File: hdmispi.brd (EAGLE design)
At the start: 30.5 x 25.4 mm, 3 parts

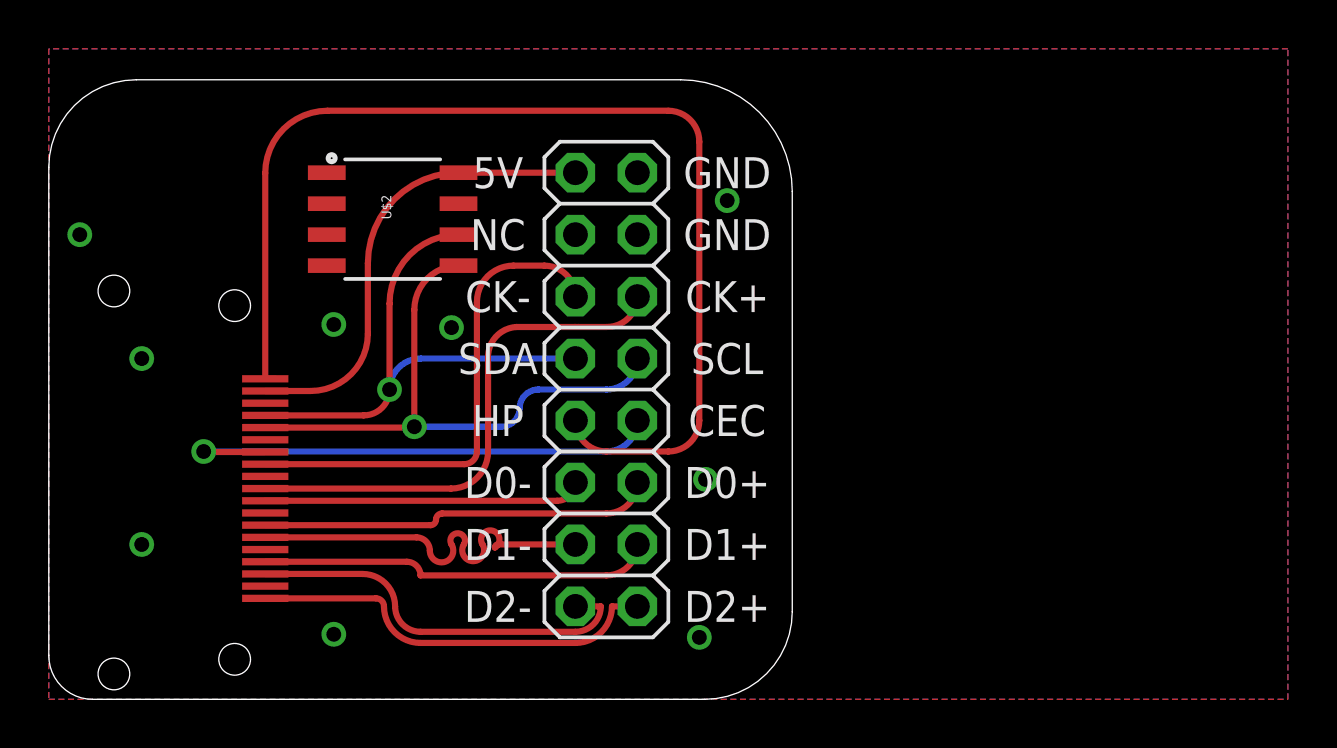
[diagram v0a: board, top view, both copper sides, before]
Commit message: next rev of files, v1.0. Switched SDA/SCL wires by accident, doesn't work.
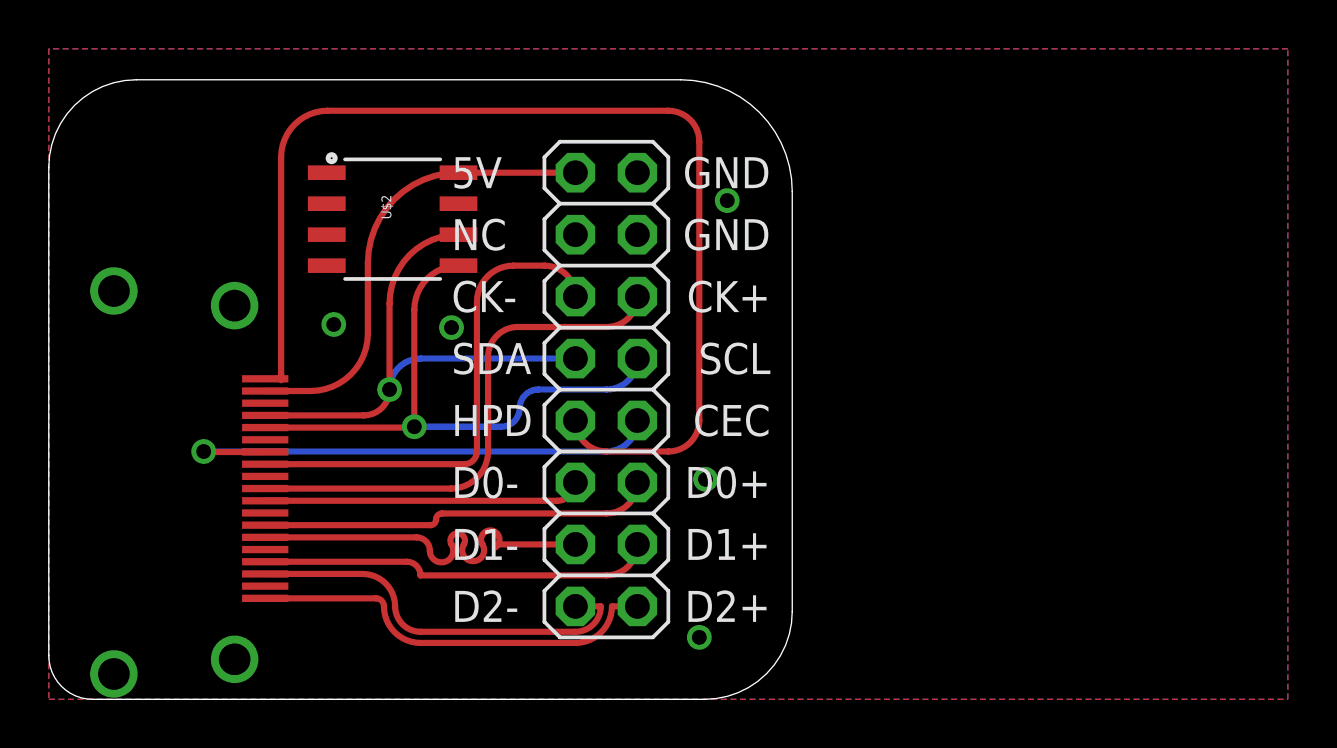
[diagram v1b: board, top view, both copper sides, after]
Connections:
- net GND: now also U$1.P$20, U$1.P$21, U$1.P$22, U$1.P$23
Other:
- board text added: "5V NC CK- SDA HPD D0- D1- D2-"
- board text added: "joefitz@securinghardware.com HDMI Breakout v1.0 W/ Microchip 24LC00/SN I2C EEPROM for EDID"
- board text removed: "5V NC CK- SDA HP D0- D1- D2-"
- board text removed: "joefitz@securinghardware.com HDMI Breakout v1.0 With Microchip 24LC00/SN I2C EEPROM for EDID"
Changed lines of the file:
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@@
 <text x="10.922" y="21.336" size="1.016" layer="26" rot="MR180" align="center">joefitz@securinghardware.com
 HDMI Breakout v1.0
-With Microchip 24LC00/SN
+W/ Microchip 24LC00/SN
 I2C EEPROM for EDID</text>
-<text x="18.415" y="12.7" size="1.27" layer="25" distance="100" rot="R180" align="center">5V
+<text x="16.51" y="12.7" size="1.27" layer="25" distance="100" rot="R180" align="center-right">5V
 NC
 CK-
 SDA
-HP
+HPD
 D0-
 D1-
 D2-</text>
-<text x="27.813" y="12.7" size="1.27" layer="25" distance="100" rot="R180" align="center">GND
+<text x="29.591" y="12.7" size="1.27" layer="25" distance="100" rot="R180" align="center-left">GND
 GND
 CK+
@@
 </polygon>
 <via x="26.67" y="2.54" extent="1-16" drill="0.6096" shape="square"/>
-<via x="3.81" y="6.35" extent="1-16" drill="0.6096" shape="square"/>
-<via x="3.81" y="13.97" extent="1-16" drill="0.6096" shape="square"/>
-<via x="1.27" y="19.05" extent="1-16" drill="0.6096" shape="square"/>
 <via x="16.51" y="15.24" extent="1-16" drill="0.6096" shape="square"/>
 <via x="27.813" y="20.447" extent="1-16" drill="0.6096" shape="square"/>
 <via x="11.684" y="15.367" extent="1-16" drill="0.6096" shape="square"/>
-<via x="11.684" y="2.667" extent="1-16" drill="0.6096" shape="square"/>
 <via x="26.924" y="9.017" extent="1-16" drill="0.6096" shape="square"/>
 <contactref element="U$2" pad="4"/>
+<contactref element="U$1" pad="P$23"/>
+<contactref element="U$1" pad="P$22"/>
+<contactref element="U$1" pad="P$21"/>
+<contactref element="U$1" pad="P$20"/>
 </signal>
 <signal name="TMDSC_N">
@@
 <wire x1="25.4" y1="24.13" x2="11.43" y2="24.13" width="0.254" layer="1"/>
 <wire x1="8.874" y1="13.14" x2="9.33" y2="13.14" width="0.254" layer="1"/>
-<wire x1="11.43" y1="24.13" x2="8.874" y2="21.574" width="0.254" layer="1" curve="90"/>
-<wire x1="8.874" y1="21.574" x2="8.874" y2="13.14" width="0.254" layer="1"/>
+<wire x1="11.43" y1="24.13" x2="9.525" y2="22.225" width="0.254" layer="1" curve="90"/>
+<wire x1="9.525" y1="22.225" x2="9.525" y2="13.97" width="0.254" layer="1"/>
+<wire x1="9.525" y1="13.335" x2="9.525" y2="13.081" width="0.254" layer="1"/>
+<wire x1="9.33" y1="13.14" x2="9.525" y2="13.335" width="0.254" layer="1" curve="90"/>
+<wire x1="9.525" y1="13.335" x2="9.525" y2="13.97" width="0.254" layer="1"/>
 </signal>
 <signal name="TMDS0_N">

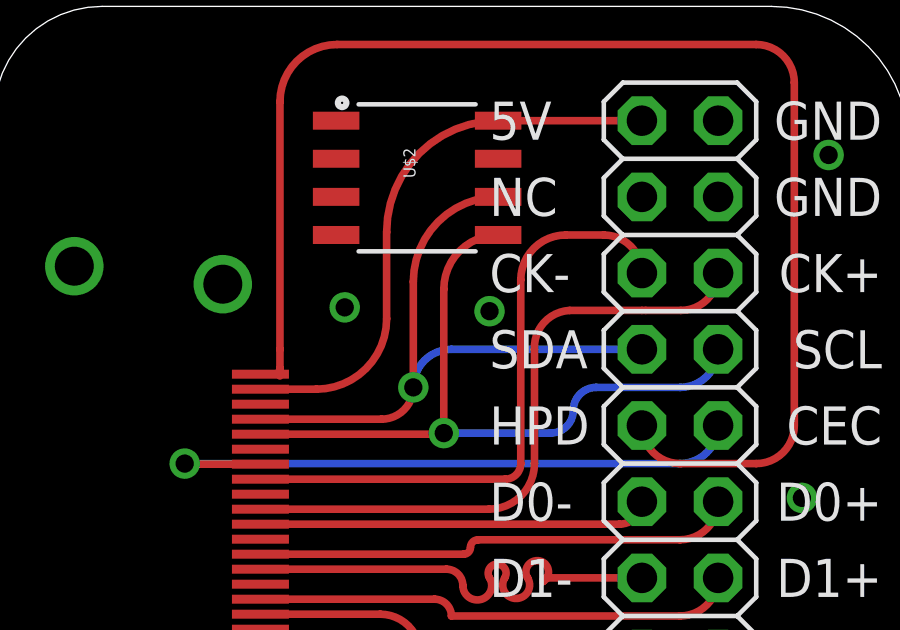
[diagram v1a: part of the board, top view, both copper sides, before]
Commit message: fixed board and schematic with sda/scl corrected.
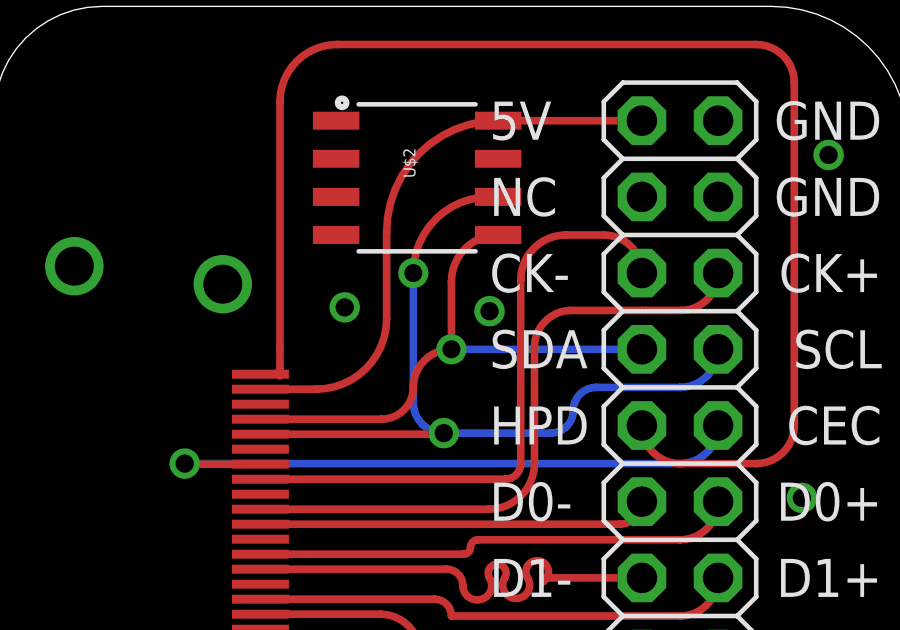
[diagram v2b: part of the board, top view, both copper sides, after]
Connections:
- net DDC_CK: now also U$2.6; no longer U$2.5
- net DDC_D: now also U$2.5; no longer U$2.6
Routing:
- net DDC_D: track 21.2 -> 18.1 mm
- net DDC_CK: track 23.8 -> 26.1 mm, vias 1 -> 2
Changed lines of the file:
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@@
 <?xml version="1.0" encoding="utf-8"?>
 <!DOCTYPE eagle SYSTEM "eagle.dtd">
-<eagle version="7.2.0">
+<eagle version="7.6.0">
 <drawing>
 <settings>
@@
 <contactref element="JP1" pad="7"/>
 <contactref element="U$1" pad="P$16"/>
+<contactref element="U$2" pad="5"/>
 <wire x1="8.874" y1="11.64" x2="12.91" y2="11.64" width="0.254" layer="1"/>
 <wire x1="12.91" y1="11.64" x2="13.97" y2="12.7" width="0.254" layer="1" curve="90"/>
-<via x="13.97" y="12.7" extent="1-16" drill="0.6096" shape="square"/>
-<wire x1="13.97" y1="12.7" x2="15.24" y2="13.97" width="0.254" layer="16" curve="-90"/>
+<wire x1="13.97" y1="12.7" x2="15.24" y2="13.97" width="0.254" layer="1" curve="-90"/>
+<via x="15.24" y="13.97" extent="1-16" drill="0.6" shape="square"/>
 <wire x1="15.24" y1="13.97" x2="21.59" y2="13.97" width="0.254" layer="16"/>
-<contactref element="U$2" pad="6"/>
-<wire x1="16.797" y1="19.05" x2="13.97" y2="16.223" width="0.254" layer="1" curve="90"/>
-<wire x1="13.97" y1="16.223" x2="13.97" y2="12.7" width="0.254" layer="1"/>
+<wire x1="15.24" y1="13.97" x2="15.24" y2="16.223" width="0.254" layer="1"/>
+<wire x1="15.24" y1="16.223" x2="16.797" y2="17.78" width="0.254" layer="1" curve="-90"/>
 </signal>
 <signal name="DDC_CK">
@@
 <wire x1="8.874" y1="11.14" x2="14.95" y2="11.14" width="0.254" layer="1"/>
 <wire x1="14.95" y1="11.14" x2="14.986" y2="11.176" width="0.254" layer="1"/>
-<contactref element="U$2" pad="5"/>
-<wire x1="16.797" y1="17.78" x2="14.986" y2="15.969" width="0.254" layer="1" curve="90"/>
-<wire x1="14.986" y1="15.969" x2="14.986" y2="11.176" width="0.254" layer="1"/>
+<contactref element="U$2" pad="6"/>
+<wire x1="14.986" y1="11.176" x2="13.97" y2="12.192" width="0.254" layer="16" curve="-90"/>
+<wire x1="13.97" y1="12.192" x2="13.97" y2="16.51" width="0.254" layer="16"/>
+<via x="13.97" y="16.51" extent="1-16" drill="0.6" shape="square"/>
+<wire x1="13.97" y1="16.51" x2="16.51" y2="19.05" width="0.254" layer="1" curve="-90"/>
+<wire x1="16.51" y1="19.05" x2="16.797" y2="19.05" width="0.254" layer="1"/>
 </signal>
 <signal name="CEC">
